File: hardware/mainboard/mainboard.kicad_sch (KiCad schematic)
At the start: 124 parts, among them J1 USB 2.0, J10 EXP1, J11 EXP2, J23 JST XH, J24 JST XH, J25 JST XH, J26 JST XH, J27 JST XH, J3 JST XH, J4 JST XH, J5 JST XH, J6 JST XH, J9 Power In, Q1 AGM308MBP, SW13 SW_SPDT, SW14 SW_SPDT, SW2 Reset, SW9 SW_SPDT, U1 STM32F407VGTx, U11 LM5160A, U12 CD40109B, U13 CD40109B, U14 LTV-357T, U15 AMS1117-3.3, U8 LM5160A, U9 CD40109B, Y1 12 MHz

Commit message: redoing board for version alpha 0.2
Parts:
- removed C10 (x2): 100nF, AlphaLib:0402C, symbol Device:C_Small
- removed C10 (x4): 1μF 50V, AlphaLib:0603C, symbol Device:C_Small
- removed C10 (x2): 10nF, AlphaLib:0402C, symbol Device:C_Small
- removed C10 (x3): 220nF, AlphaLib:0402C, symbol Device:C_Small
- removed C10 (x2): 1μF, AlphaLib:0402C, symbol Device:C_Small
- removed C10 (x2): 1nF, AlphaLib:0402C, symbol Device:C_Small
- removed C10 (x2): 50nF, AlphaLib:0402C, symbol Device:C_Small
- removed C10 (x2): 22μF, Capacitor_SMD:C_0805_2012Metric, symbol Device:C_Small
- removed C10 (x2): 2.2μF, AlphaLib:0402C, symbol Device:C_Small
- removed C10: 20pF, AlphaLib:0402C, symbol Device:C_Small
- removed C10 (x2): 3.3nF, AlphaLib:0402C, symbol Device:C_Small
- removed D1 (x2): G, AlphaLib:0603LED, symbol Device:LED_Small
- removed D1 (x2): A, AlphaLib:0603LED, symbol Device:LED_Small
- removed F3: Fuse, corevus:XF-508P-B, symbol Device:Fuse
- removed J11: EXP2, Connector_IDC:IDC-Header_2x05_P2.54mm_Vertical, symbol Connector_Generic:Conn_02x05_Odd_Even
- removed L1, L2: 15μH/3A, Inductor_SMD:L_Chilisin_BMRB00060618, symbol Device:L
- removed R3 (x2): 10kΩ, AlphaLib:0402R, symbol Device:R_Small
- removed R3 (x4): 150kΩ, AlphaLib:0402R, symbol Device:R_Small
- removed R3: 3.3kΩ, AlphaLib:0402R, symbol Device:R_Small
- removed R3 (x2): 100kΩ, AlphaLib:0402R, symbol Device:R_Small
- removed R3 (x2): 51kΩ, AlphaLib:0402R, symbol Device:R_Small
- removed R3 (x4): 1kΩ, AlphaLib:0402R, symbol Device:R_Small
- removed R3: 5.1kΩ, AlphaLib:0402R, symbol Device:R_Small
- removed R3: 2.2kΩ, AlphaLib:0402R, symbol Device:R_Small
- removed R3: 200Ω, AlphaLib:0402R, symbol Device:R_Small
- removed R3: 220kΩ, AlphaLib:0402R, symbol Device:R_Small
- removed SW14: SW_SPDT, corevus:MSS12C02-LS, symbol Switch:SW_SPDT
- removed SW2: Reset, Button_Switch_SMD:SW_SPST_SKQG_WithStem, symbol Switch:SW_Push
- removed U1: STM32F407VGTx, Package_QFP:LQFP-100_14x14mm_P0.5mm, symbol MCU_ST_STM32F4:STM32F407VGTx
- removed U11, U8: LM5160A, Package_SON:WSON-12-1EP_4x4mm_P0.5mm_EP2.6x3mm_ThermalVias, symbol corevus:LM5160A
- added C10 (x2): 2.2μF, AlphaLib:0402C, symbol Device:C_Small
- added C10: 20pF, AlphaLib:0402C, symbol Device:C_Small
- added D1: Red, AlphaLib:0402LED, symbol Device:LED_Small
- added F6: 10A, corevus:XF-505P, symbol Device:Fuse
- added J13: EXP2, corevus:IDC-Header_2x05_P2.54mm_Vertical_SMD, symbol Connector_Generic:Conn_02x05_Odd_Even
- added R3: 330Ω, AlphaLib:0402R, symbol Device:R_Small
- added R3: 100kΩ, AlphaLib:0402R, symbol Device:R_Small
- added R3: 10kΩ, AlphaLib:0402R, symbol Device:R_Small
- added SW1: SW_SPDT, corevus:MSS12C02-LS, symbol Switch:SW_SPDT
- added U1: STM32F407ZETx, Package_QFP:LQFP-144_20x20mm_P0.5mm, symbol MCU_ST_STM32F4:STM32F407ZETx
- D1: value A -> Red; footprint AlphaLib:0603LED -> AlphaLib:0402LED
- F1, F2, F4, F5: value Fuse -> 10A; footprint corevus:XF-508P-B -> corevus:XF-505P
- F3: renamed from F6; footprint corevus:XF-508P-B -> corevus:XF-505P
- J12: renamed from J10; footprint Connector_IDC:IDC-Header_2x05_P2.54mm_Vertical -> corevus:IDC-Header_2x05_P2.54mm_Vertical_SMD
- renumbered C6 to C12, C27 to C13, C9 to C14, C8 to C15, C33 to C16, C7 to C17, J26 to J10, J27 to J11, J24 to J2, J9 to J3, J3 to J4, J4 to J6, J6 to J7, J23 to J8, J25 to J9, SW13 to SW2, U13 to U2, U12 to U3, U9 to U4, U14 to U5, U15 to U6
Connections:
- net +24V: now also F6.1; no longer F1.2
- net +3.3V: now also SW1.3 (C), U1.108 (VDD), U1.121 (VDD), U1.131 (VDD), U1.144 (VDD), U1.17 (VDD), U1.30 (VDD), U1.32 (VREF+), U1.33 (VDDA), U1.39 (VDD), U1.52 (VDD), U1.6 (VBAT), U1.62 (VDD), U1.72 (VDD), U1.84 (VDD), U1.95 (VDD); no longer U2.15 (En_{D}), U2.9 (En_{C}), U3.15 (En_{D}), U3.9 (En_{C}), U4.15 (En_{D}), U4.9 (En_{C})
- net +48V: no longer F5.1, J3.2 (Pin_2)
- net +5V: now also J13.10 (Pin_10)
- net BG: now also U4.13 (H); no longer SW9.2 (B)
- net BOOT0: now also D1.2 (A), R3.1, SW1.2 (B), U1.138 (BOOT0)
- net Btn_En1: now also J13.5 (Pin_5)
- net Btn_En2: now also J13.3 (Pin_3)
- net GND: now also C10.1, C10.2, C10.2, J13.9 (Pin_9), R3.1, R3.2, SW1.1 (A), U1.107 (VSS), U1.120 (VSS), U1.130 (VSS), U1.16 (VSS), U1.31 (VSSA), U1.38 (VSS), U1.51 (VSS), U1.61 (VSS), U1.83 (VSS), U1.94 (VSS); no longer SW9.3 (C)
- net MISO_{3}: now also J13.1 (Pin_1)
- net MOSI_{3}: now also J13.6 (Pin_6)
- net SClk_{3}: now also J13.2 (Pin_2)
- net SD_CS: now also J13.4 (Pin_4)
- net SD_Det: now also J13.7 (Pin_7)
- net VMB: now also F4.1, F5.1; no longer F2.2
- net VMC: now also F1.1, F2.1; no longer F4.2, F5.2
- net ~{Reset}: now also J13.8 (Pin_8)
- net at C10.2, Y1.3: now also R3.2, U1.24 (PH1)
- net at Y1.1: now also C10.2, R3.1, U1.23 (PH0)
- net Bed_Gate: no longer names the net of SW9.1 (A)
- net Bed_Gate: no longer U4.13 (H)
- net USB_D+: no longer names the net of R3.1
- net USB_D+: now also U1.104 (PA12)
- net USB_D-: no longer names the net of R3.1
- net USB_D-: now also U1.103 (PA11)
- new net: F2.2, F3.2, F5.2, F6.2, J3.4 (Pin_4)
- new net: F1.2, F4.2, J3.2 (Pin_2)
- new net: D1.1 (K), R3.2
- new net: C10.1, U1.106 (VCAP_2)
- new net: C10.1, U1.71 (VCAP_1)
- new net HeEn: U2.15 (En_{D}), U2.9 (En_{C}), U3.15 (En_{D}), U3.9 (En_{C}), U4.15 (En_{D}), U4.9 (En_{C})
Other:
- note removed: "Mechanical switch hard-cutoffs gate drive signal and shorts it to ground."
- moved on the sheet: C10, D1, F3, J1, J2, Q1A, Q1B, R3, SW2, U5

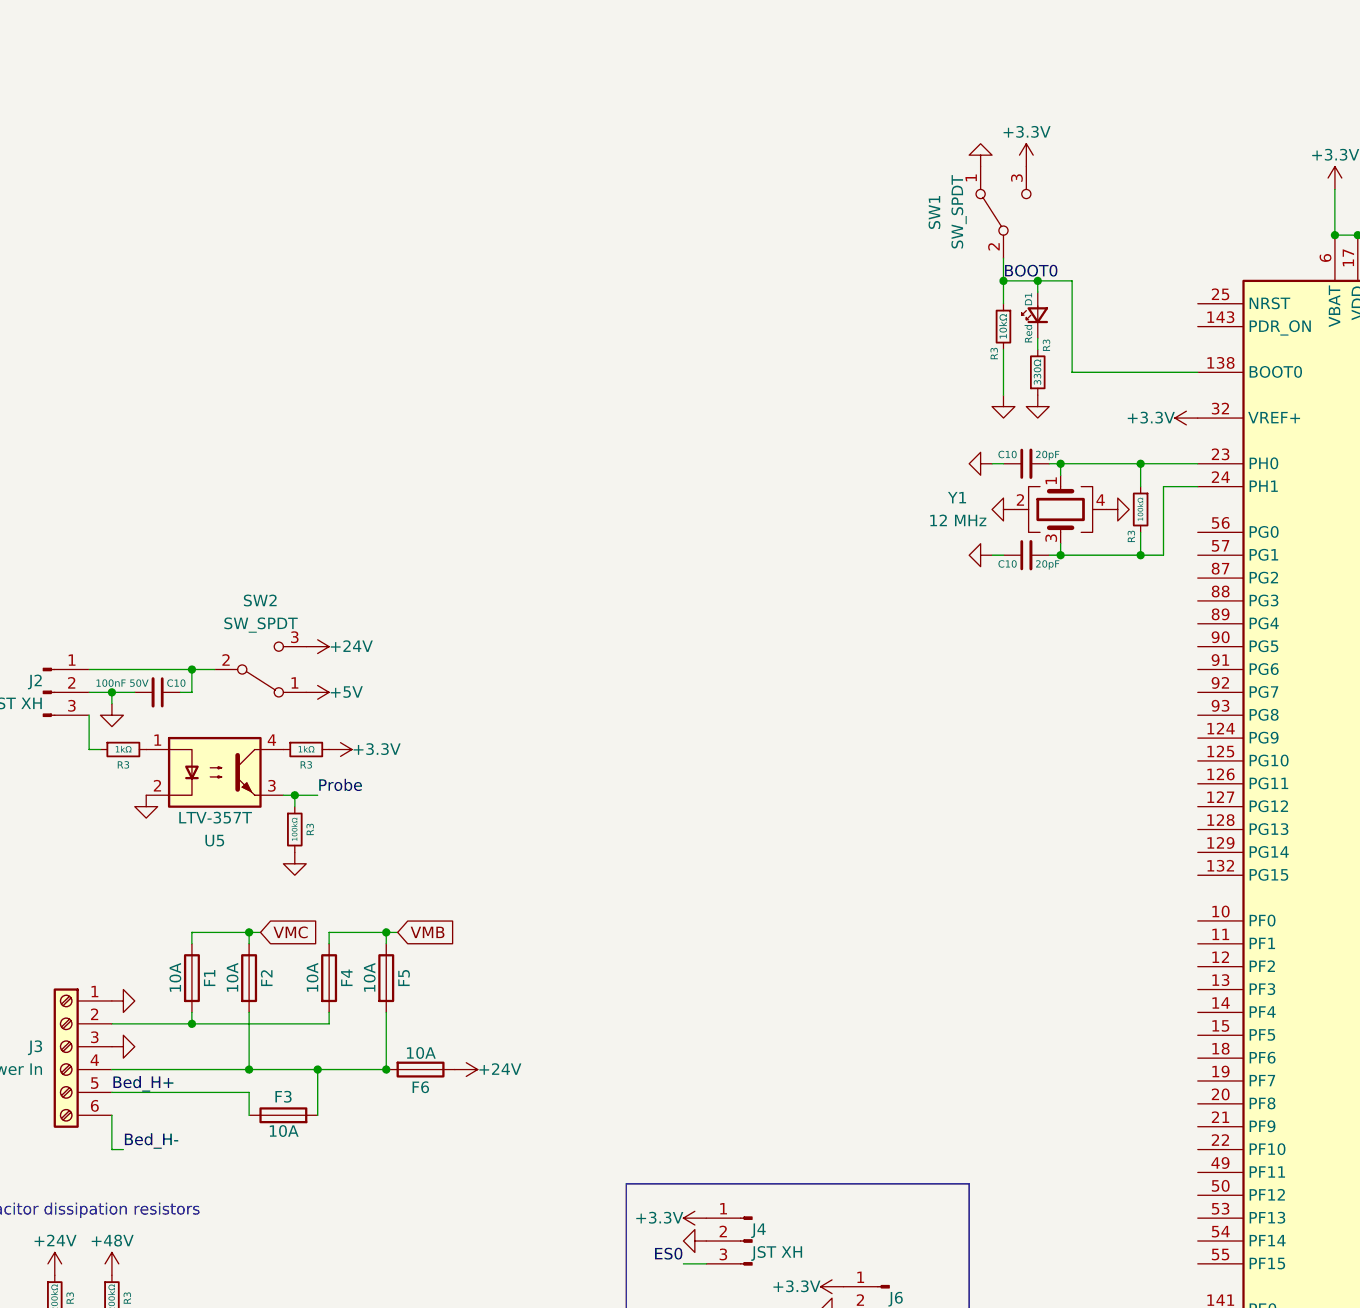
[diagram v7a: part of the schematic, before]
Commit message: added components and further work on PCB layout design
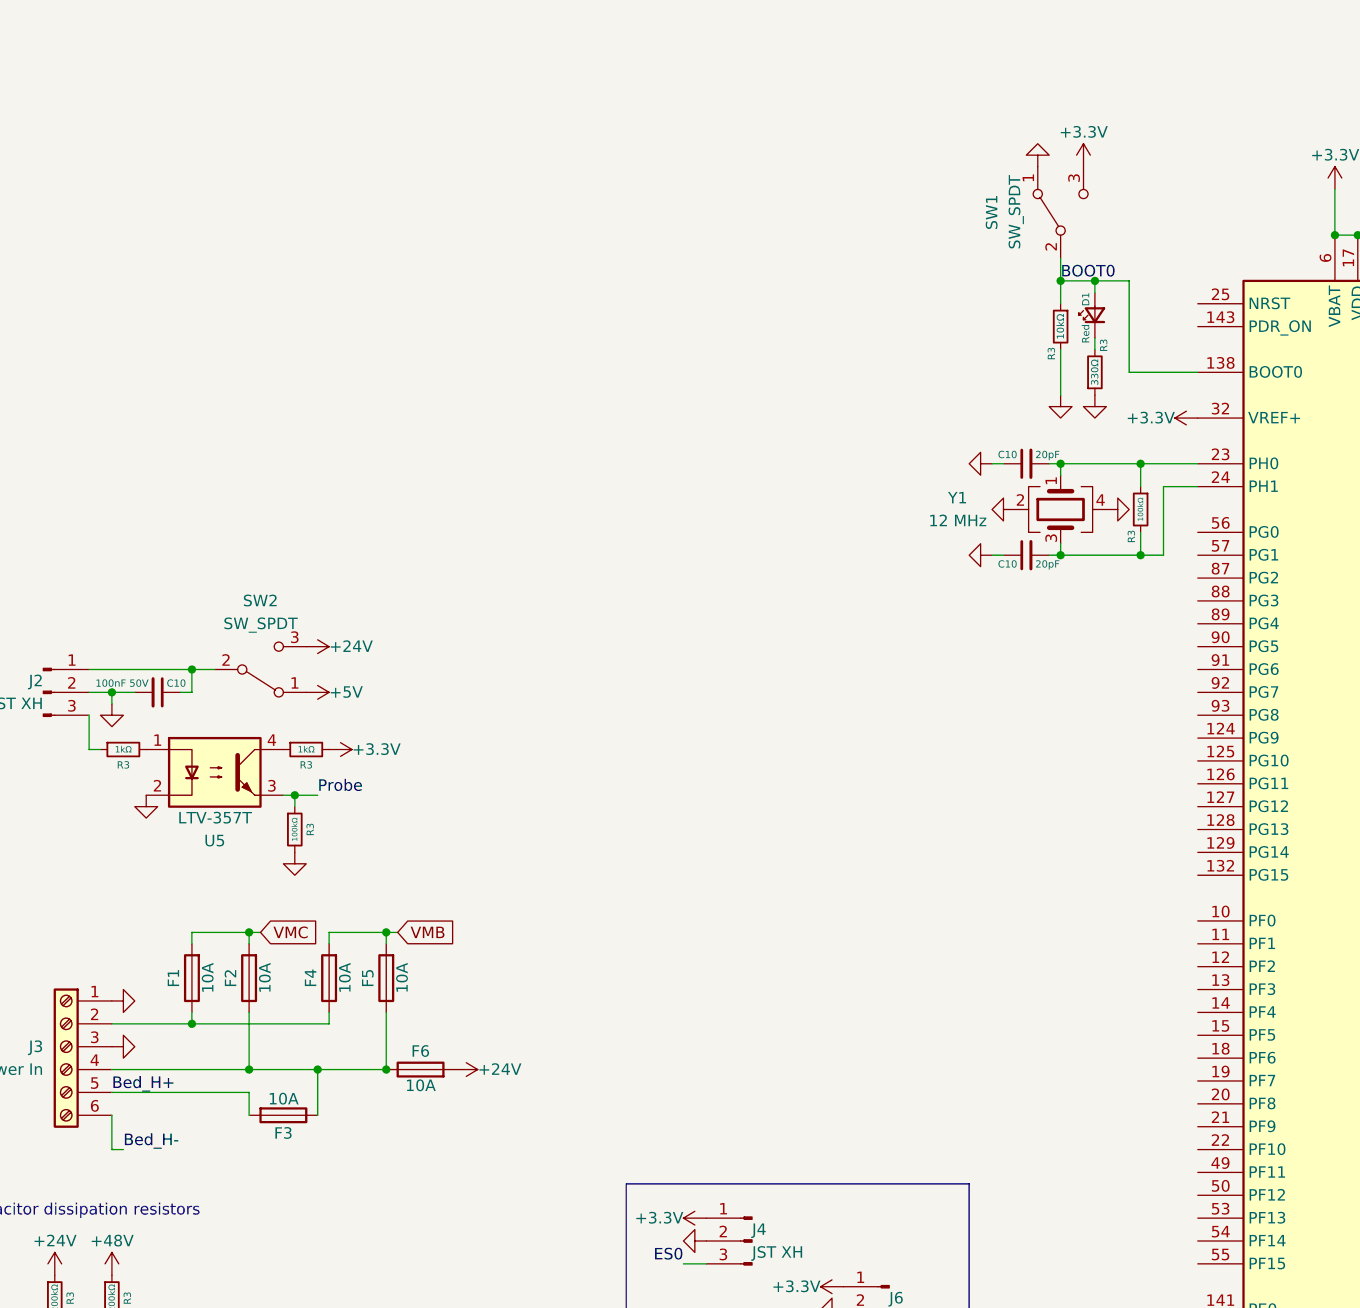
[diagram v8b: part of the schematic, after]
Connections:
- net +24V: now also F6.2; no longer F6.1
- net Bed_H+: now also F3.2; no longer F3.1
- net VMB: now also F4.2, F5.2; no longer F4.1, F5.1
- net VMC: now also F1.2, F2.2; no longer F1.1, F2.1
- new net: F2.1, F3.1, F5.1, F6.1, J3.4 (Pin_4)
- new net: F1.1, F4.1, J3.2 (Pin_2)
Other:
- moved on the sheet: D1, F1, F2, F3, F4, F5, F6, R3, SW1
